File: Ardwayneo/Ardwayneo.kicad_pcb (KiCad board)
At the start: 2 copper layers, 0 parts

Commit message: Setup layout, added track, via, drill presets in design rules
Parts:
- added BT1: Battery 3V, Connector_PinHeader_2.54mm:PinHeader_1x02_P2.54mm_Vertical, F.Cu at (114.0, 65.5)
- added C1: 22pF, Connector_PinHeader_2.54mm:PinHeader_1x09_P2.54mm_Vertical, F.Cu at (98.3, 71.9)
- added C2: 22pF, Connector_PinHeader_2.54mm:PinHeader_1x09_P2.54mm_Vertical, F.Cu at (103.0, 71.9)
- added C3: 10µF, Connector_PinHeader_2.54mm:PinHeader_1x09_P2.54mm_Vertical, F.Cu at (107.6, 71.9)
- added D1: LED, LED_SMD:LED_0805_2012Metric_Pad1.15x1.40mm_HandSolder, F.Cu at (167.1, 88.9)
- added J1: Digital Pins, Connector_PinHeader_2.54mm:PinHeader_1x09_P2.54mm_Vertical, F.Cu at (98.3, 102.4)
- added J2: ICSP, Connector_PinSocket_2.54mm:PinSocket_2x03_P2.54mm_Vertical, F.Cu at (114.7, 102.4)
- added J3: Serial, Connector_PinSocket_2.54mm:PinSocket_1x04_P2.54mm_Vertical, F.Cu at (103.0, 102.4)
- added J4: I²C, Connector_PinSocket_2.54mm:PinSocket_1x04_P2.54mm_Vertical, F.Cu at (107.6, 102.4)
- added R1: 330Ω, Resistor_SMD:R_0805_2012Metric_Pad1.20x1.40mm_HandSolder, F.Cu at (167.0, 92.0)
- added R2: 10KΩ, Resistor_SMD:R_0805_2012Metric_Pad1.20x1.40mm_HandSolder, F.Cu at (172.1, 85.4)
- added U1: 24LC1025, Package_SO:SOIJ-8_5.3x5.3mm_P1.27mm, F.Cu at (170.9, 75.6)
- added U2: 24LC1025, Package_SO:SOIJ-8_5.3x5.3mm_P1.27mm, F.Cu at (159.4, 87.1)
- added U3: ATMEGA328P-AU, digikey-footprints:TQFP-32_7x7mm, F.Cu at (159.9, 77.9)
- added U?1: DS1337S+, Package_SO:SO-8_5.3x6.2mm_P1.27mm, F.Cu at (159.4, 94.4)
- added Y1: Crystal 32MHz, Crystal:Crystal_SMD_MicroCrystal_CC7V-T1A-2Pin_3.2x1.5mm, F.Cu at (167.2, 85.7)
- added Y2: Crystal 16MHz, Crystal:Crystal_SMD_5032-2Pin_5.0x3.2mm_HandSoldering, F.Cu at (170.7, 81.5)
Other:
- net class Power added: clearance 0.2, trace_width 0.3, via_dia 1, via_drill 0.6

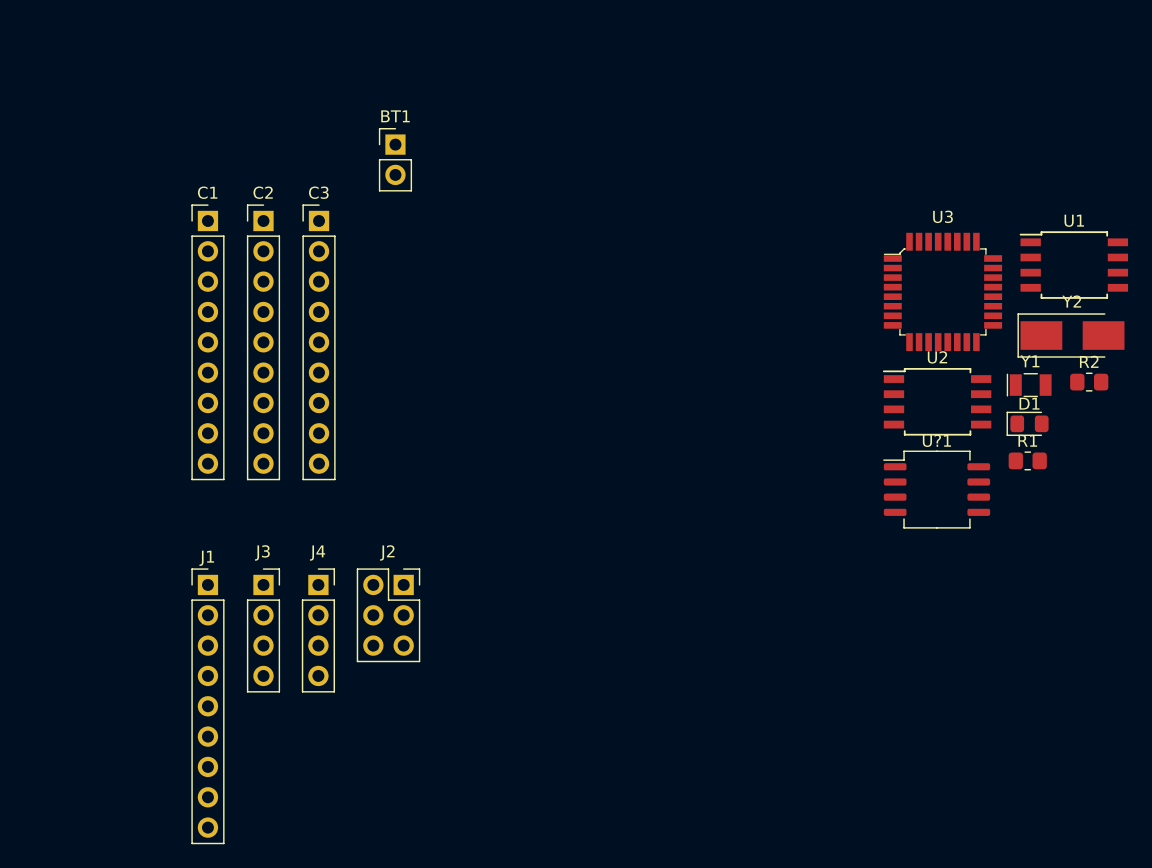
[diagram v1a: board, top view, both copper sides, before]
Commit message: Fixed association for capacitor footprints
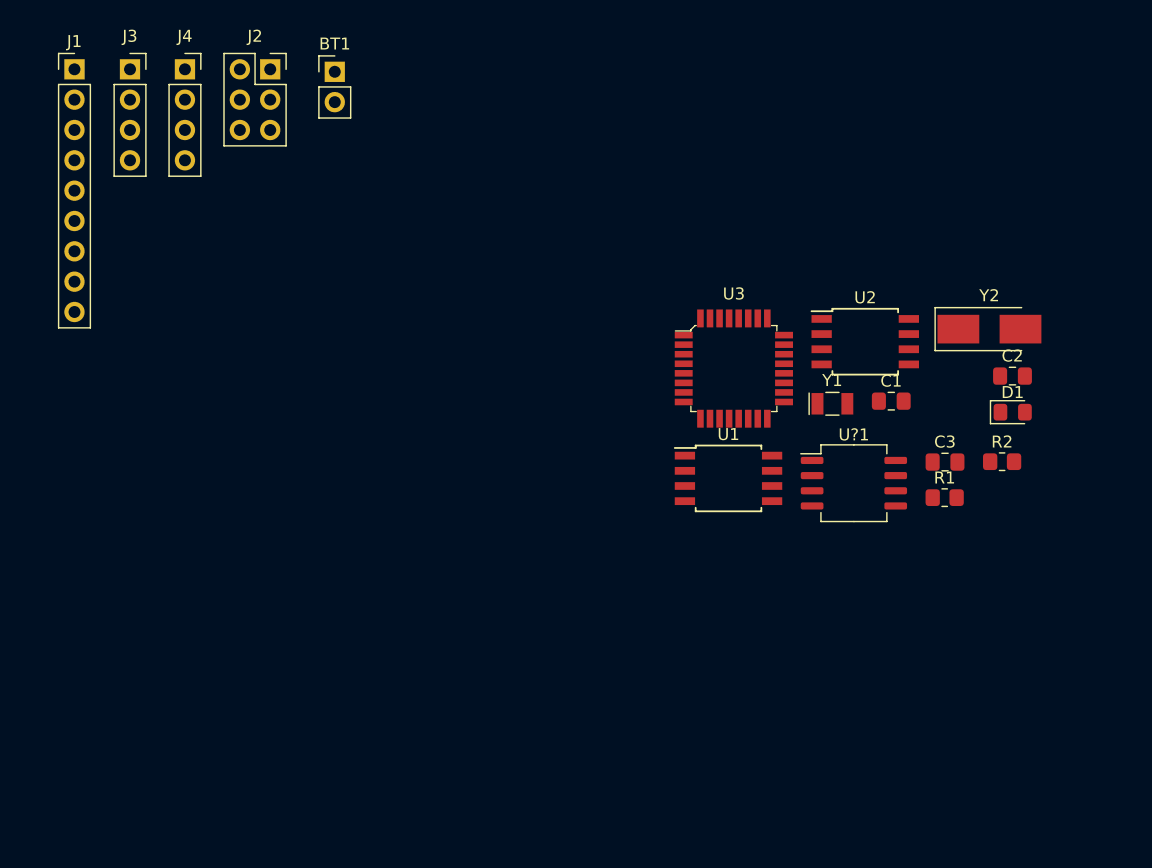
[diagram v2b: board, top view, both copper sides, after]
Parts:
- C1, C2, C3: footprint Connector_PinHeader_2.54mm:PinHeader_1x09_P2.54mm_Vertical -> Capacitor_SMD:C_0805_2012Metric_Pad1.18x1.45mm_HandSolder
- moved C2 64.1 mm to (165.7, 84.9)
- moved C1 59.2 mm to (155.6, 87.0)
- moved C3 56.2 mm to (160.1, 92.1)
- moved J1 44.6 mm to (87.2, 59.2)
- moved J2 44.6 mm to (103.6, 59.2)
- moved J3 44.6 mm to (91.8, 59.2)
- moved J4 44.6 mm to (96.4, 59.2)
- moved U1 34.0 mm to (141.9, 93.5)
- moved U3 18.6 mm to (142.4, 84.3)
- moved Y1 16.7 mm to (150.6, 87.2)
- moved R2 9.88 mm to (164.8, 92.1)
- moved BT1 7.94 mm to (109.0, 59.4)
- moved U2 7.88 mm to (153.4, 82.0)
- moved R1 7.61 mm to (160.0, 95.1)
- moved Y2 6.98 mm to (163.8, 81.0)
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
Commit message: Initial layout distribution
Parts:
- moved R2 76.2 mm to (88.9, 86.4), turned to 90 degrees
- moved Y2 67.7 mm to (96.3, 86.3)
- moved C2 61.3 mm to (104.4, 85.4)
- moved C1 51.2 mm to (104.4, 88.4)
- moved U3 46.8 mm to (97.0, 95.8)
- moved J1 46.2 mm to (95.5, 104.6), turned to 90 degrees
- moved U2 41.4 mm to (112.5, 88.9)
- moved D1 41.1 mm to (126.5, 100.1)
- moved R1 39.2 mm to (121.2, 100.1)
- moved C3 39.1 mm to (121.1, 96.2), turned to 180 degrees
- moved J2 38.7 mm to (87.1, 94.2)
- moved BT1 35.4 mm to (84.6, 85.1)
- moved U1 29.8 mm to (112.5, 98.1)
- moved U3 29.1 mm to (123.7, 89.3)
- moved J4 27.7 mm to (112.8, 81.5), turned to 90 degrees
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- renumbered U?1 to U3

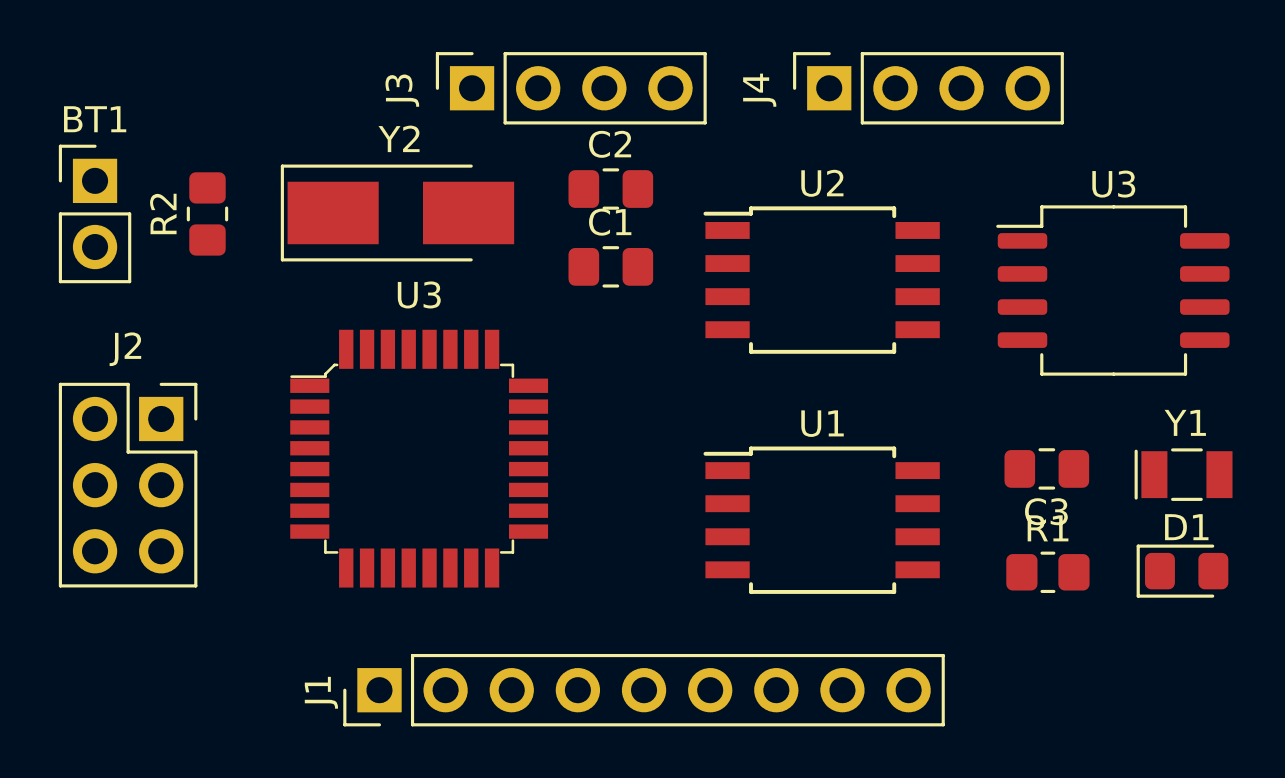
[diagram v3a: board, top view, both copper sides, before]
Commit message: Refined, condensed layout
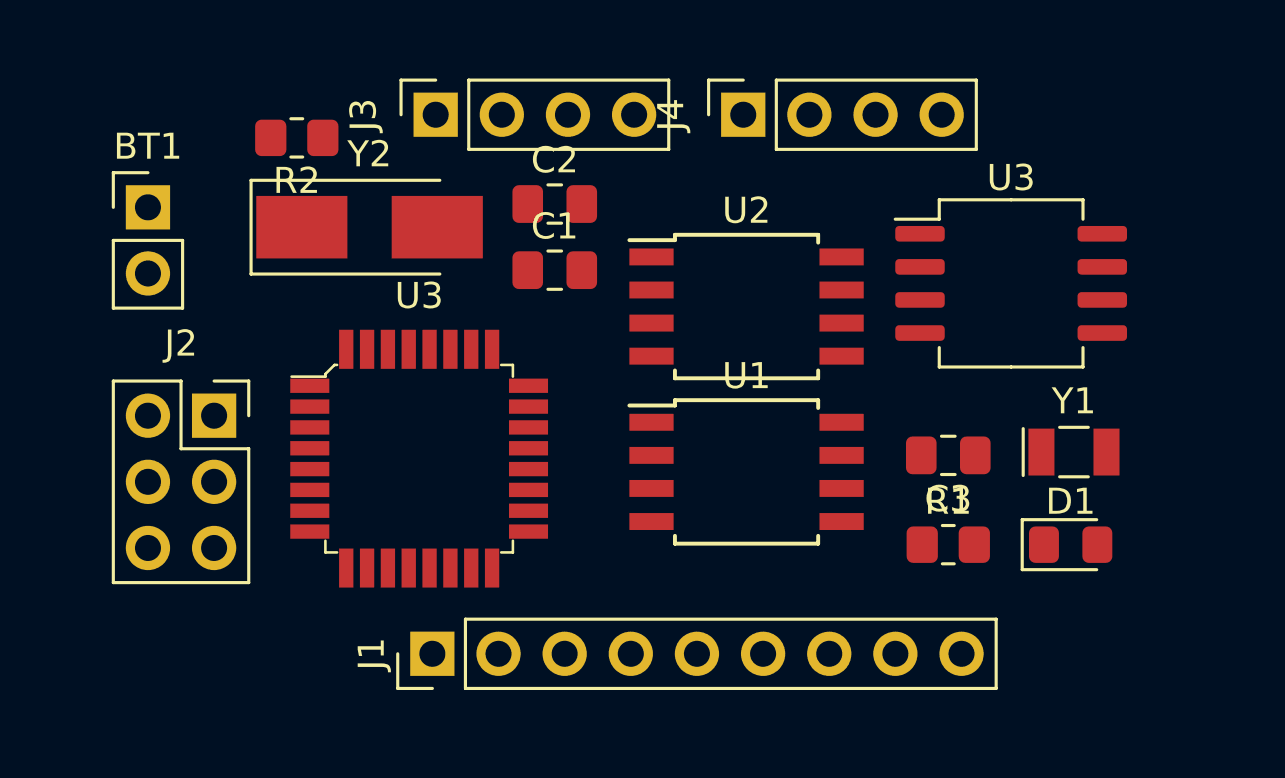
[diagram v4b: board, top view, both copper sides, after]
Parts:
- J4: value I²C -> I2C
- moved D1 4.57 mm to (122.0, 99.1)
- moved R2 4.50 mm to (92.3, 83.4), turned to 180 degrees
- moved Y1 4.42 mm to (122.2, 95.5)
- moved R1 3.97 mm to (117.3, 99.1)
- moved U3 3.95 mm to (119.8, 89.0)
- moved C3 3.82 mm to (117.3, 95.6)
- moved U1 3.46 mm to (109.6, 96.3)
- moved J4 3.45 mm to (109.5, 82.5)
- moved U2 3.09 mm to (109.6, 89.9)
- moved J1 2.47 mm to (97.5, 103.3)
- moved BT1 2.27 mm to (86.6, 86.1)
- moved C2 2.23 mm to (102.2, 86.0)
- moved C1 2.16 mm to (102.2, 88.5)
- moved J2 2.04 mm to (89.2, 94.1)
- moved J3 1.73 mm to (97.7, 82.5)
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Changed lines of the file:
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@@
   )
   (module Connector_PinHeader_2.54mm:PinHeader_1x02_P2.54mm_Vertical (layer F.Cu)
-    (at 84.582 85.09)
+    (at 86.614 86.106)
     (descr "Through hole straight pin header, 1x02, 2.54mm pitch, single row")
     (tags "Through hole pin header THT 1x02 2.54mm single row")
@@
   )
   (module Capacitor_SMD:C_0805_2012Metric_Pad1.18x1.45mm_HandSolder (layer F.Cu)
-    (at 104.389499 88.392)
+    (at 102.235 88.519)
     (descr "Capacitor SMD 0805 (2012 Metric), square (rectangular) end terminal, IPC_7351 nominal with elongated pad for handsoldering. (Body size source: IPC-SM-782 page 76, https://www.pcb-3d.com/wordpress/wp-content/uploads/ipc-sm-782a_amendment_1_and_2.pdf, https://docs.google.com/spreadsheets/d/1BsfQQcO9C6DZCsRaXUlFlo91Tg2WpOkGARC1WS5S8t0/edit?usp=sharing), generated with kicad-footprint-generator")
     (tags "capacitor handsolder")
@@
   )
   (module Capacitor_SMD:C_0805_2012Metric_Pad1.18x1.45mm_HandSolder (layer F.Cu)
-    (at 104.389499 85.403001)
+    (at 102.235 85.979)
     (descr "Capacitor SMD 0805 (2012 Metric), square (rectangular) end terminal, IPC_7351 nominal with elongated pad for handsoldering. (Body size source: IPC-SM-782 page 76, https://www.pcb-3d.com/wordpress/wp-content/uploads/ipc-sm-782a_amendment_1_and_2.pdf, https://docs.google.com/spreadsheets/d/1BsfQQcO9C6DZCsRaXUlFlo91Tg2WpOkGARC1WS5S8t0/edit?usp=sharing), generated with kicad-footprint-generator")
     (tags "capacitor handsolder")
@@
   )
   (module Capacitor_SMD:C_0805_2012Metric_Pad1.18x1.45mm_HandSolder (layer F.Cu)
-    (at 121.132 96.151 180)
+    (at 117.348 95.631 180)
     (descr "Capacitor SMD 0805 (2012 Metric), square (rectangular) end terminal, IPC_7351 nominal with elongated pad for handsoldering. (Body size source: IPC-SM-782 page 76, https://www.pcb-3d.com/wordpress/wp-content/uploads/ipc-sm-782a_amendment_1_and_2.pdf, https://docs.google.com/spreadsheets/d/1BsfQQcO9C6DZCsRaXUlFlo91Tg2WpOkGARC1WS5S8t0/edit?usp=sharing), generated with kicad-footprint-generator")
     (tags "capacitor handsolder")
@@
   )
   (module LED_SMD:LED_0805_2012Metric_Pad1.15x1.40mm_HandSolder (layer F.Cu)
-    (at 126.501 100.076)
+    (at 122.047 99.06)
     (descr "LED SMD 0805 (2012 Metric), square (rectangular) end terminal, IPC_7351 nominal, (Body size source: https://docs.google.com/spreadsheets/d/1BsfQQcO9C6DZCsRaXUlFlo91Tg2WpOkGARC1WS5S8t0/edit?usp=sharing), generated with kicad-footprint-generator")
     (tags "LED handsolder")
@@
   )
   (module Connector_PinHeader_2.54mm:PinHeader_1x09_P2.54mm_Vertical (layer F.Cu)
-    (at 95.504 104.648 90)
+    (at 97.536 103.251 90)
     (descr "Through hole straight pin header, 1x09, 2.54mm pitch, single row")
     (tags "Through hole pin header THT 1x09 2.54mm single row")
@@
   )
   (module Connector_PinSocket_2.54mm:PinSocket_2x03_P2.54mm_Vertical (layer F.Cu)
-    (at 87.122 94.234)
+    (at 89.154 94.107)
     (descr "Through hole straight socket strip, 2x03, 2.54mm pitch, double cols (from Kicad 4.0.7), script generated")
     (tags "Through hole socket strip THT 2x03 2.54mm double row")
@@
   )
   (module Connector_PinSocket_2.54mm:PinSocket_1x04_P2.54mm_Vertical (layer F.Cu)
-    (at 99.06 81.534 90)
+    (at 97.663 82.55 90)
     (descr "Through hole straight socket strip, 1x04, 2.54mm pitch, single row (from Kicad 4.0.7), script generated")
     (tags "Through hole socket strip THT 1x04 2.54mm single row")
@@
   )
   (module Connector_PinSocket_2.54mm:PinSocket_1x04_P2.54mm_Vertical (layer F.Cu)
-    (at 112.776 81.534 90)
+    (at 109.474 82.55 90)
     (descr "Through hole straight socket strip, 1x04, 2.54mm pitch, single row (from Kicad 4.0.7), script generated")
     (tags "Through hole socket strip THT 1x04 2.54mm single row")
@@
       (effects (font (size 1 1) (thickness 0.15)))
     )
-    (fp_text value I²C (at 0 10.39 90) (layer F.Fab)
+    (fp_text value I2C (at 0 10.39 90) (layer F.Fab)
       (effects (font (size 1 1) (thickness 0.15)))
     )
@@
   )
   (module Resistor_SMD:R_0805_2012Metric_Pad1.20x1.40mm_HandSolder (layer F.Cu)
-    (at 121.174 100.121)
+    (at 117.348 99.06)
     (descr "Resistor SMD 0805 (2012 Metric), square (rectangular) end terminal, IPC_7351 nominal with elongated pad for handsoldering. (Body size source: IPC-SM-782 page 72, https://www.pcb-3d.com/wordpress/wp-content/uploads/ipc-sm-782a_amendment_1_and_2.pdf), generated with kicad-footprint-generator")
     (tags "resistor handsolder")
@@
   )
   (module Resistor_SMD:R_0805_2012Metric_Pad1.20x1.40mm_HandSolder (layer F.Cu)
-    (at 88.9 86.36 90)
+    (at 92.329 83.439 180)
     (descr "Resistor SMD 0805 (2012 Metric), square (rectangular) end terminal, IPC_7351 nominal with elongated pad for handsoldering. (Body size source: IPC-SM-782 page 72, https://www.pcb-3d.com/wordpress/wp-content/uploads/ipc-sm-782a_amendment_1_and_2.pdf), generated with kicad-footprint-generator")
     (tags "resistor handsolder")
     (attr smd)
-    (fp_text reference R2 (at 0 -1.65 90) (layer F.SilkS)
-      (effects (font (size 1 1) (thickness 0.15)))
-    )
-    (fp_text value 10KΩ (at 0 1.65 90) (layer F.Fab)
-      (effects (font (size 1 1) (thickness 0.15)))
-    )
-    (fp_text user %R (at 0 0 90) (layer F.Fab)
+    (fp_text reference R2 (at 0 -1.65) (layer F.SilkS)
+      (effects (font (size 1 1) (thickness 0.15)))
+    )
+    (fp_text value 10KΩ (at 0 1.65) (layer F.Fab)
+      (effects (font (size 1 1) (thickness 0.15)))
+    )
+    (fp_text user %R (at 0 0) (layer F.Fab)
       (effects (font (size 0.5 0.5) (thickness 0.08)))
     )
@@
     (fp_line (start 1.85 -0.95) (end 1.85 0.95) (layer F.CrtYd) (width 0.05))
     (fp_line (start 1.85 0.95) (end -1.85 0.95) (layer F.CrtYd) (width 0.05))
-    (pad 2 smd roundrect (at 1 0 90) (size 1.2 1.4) (layers F.Cu F.Paste F.Mask) (roundrect_rratio 0.208333)
+    (pad 2 smd roundrect (at 1 0 180) (size 1.2 1.4) (layers F.Cu F.Paste F.Mask) (roundrect_rratio 0.208333)
       (net 16 /RESET))
-    (pad 1 smd roundrect (at -1 0 90) (size 1.2 1.4) (layers F.Cu F.Paste F.Mask) (roundrect_rratio 0.208333)
+    (pad 1 smd roundrect (at -1 0 180) (size 1.2 1.4) (layers F.Cu F.Paste F.Mask) (roundrect_rratio 0.208333)
       (net 1 /Vcc))
     (model ${KISYS3DMOD}/Resistor_SMD.3dshapes/R_0805_2012Metric.wrl
@@
   )
   (module Package_SO:SOIJ-8_5.3x5.3mm_P1.27mm (layer F.Cu)
-    (at 112.522 98.121)
+    (at 109.601 96.266)
     (descr "8-Lead Plastic Small Outline (SM) - Medium, 5.28 mm Body [SOIC] (see Microchip Packaging Specification 00000049BS.pdf)")
     (tags "SOIC 1.27")
@@
   )
   (module Package_SO:SOIJ-8_5.3x5.3mm_P1.27mm (layer F.Cu)
-    (at 112.522 88.9)
+    (at 109.601 89.916)
     (descr "8-Lead Plastic Small Outline (SM) - Medium, 5.28 mm Body [SOIC] (see Microchip Packaging Specification 00000049BS.pdf)")
     (tags "SOIC 1.27")
@@
   )
   (module Package_SO:SO-8_5.3x6.2mm_P1.27mm (layer F.Cu)
-    (at 123.698 89.3)
+    (at 119.761 89.027)
     (descr "SO, 8 Pin (https://www.ti.com/lit/ml/msop001a/msop001a.pdf), generated with kicad-footprint-generator ipc_gullwing_generator.py")
     (tags "SO SO")
@@
   )
   (module Crystal:Crystal_SMD_MicroCrystal_CC7V-T1A-2Pin_3.2x1.5mm (layer F.Cu)
-    (at 126.512 96.371)
+    (at 122.174 95.504)
     (descr "SMD Crystal MicroCrystal CC7V-T1A/CM7V-T1A series https://www.microcrystal.com/fileadmin/Media/Products/32kHz/Datasheet/CC7V-T1A.pdf, 3.2x1.5mm^2 package")
     (tags "SMD SMT crystal")
@@
   )
   (module Crystal:Crystal_SMD_5032-2Pin_5.0x3.2mm_HandSoldering (layer F.Cu)
-    (at 96.326 86.323001)
+    (at 95.123 86.868)
     (descr "SMD Crystal SERIES SMD2520/2 http://www.icbase.com/File/PDF/HKC/HKC00061008.pdf, hand-soldering, 5.0x3.2mm^2 package")
     (tags "SMD SMT crystal hand-soldering")

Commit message: Refined layout
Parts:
- moved U3 1.05 mm to (98.0, 95.5)
- moved J1 0.28 mm to (97.4, 103.5)
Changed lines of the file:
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@@
   )
   (module Connector_PinHeader_2.54mm:PinHeader_1x09_P2.54mm_Vertical (layer F.Cu)
-    (at 97.536 103.251 90)
+    (at 97.409 103.505 90)
     (descr "Through hole straight pin header, 1x09, 2.54mm pitch, single row")
     (tags "Through hole pin header THT 1x09 2.54mm single row")
@@
   )
   (module digikey-footprints:TQFP-32_7x7mm (layer F.Cu)
-    (at 97.028 95.758)
+    (at 98.044 95.504)
     (descr http://www.atmel.com/Images/Atmel-8826-SEEPROM-PCB-Mounting-Guidelines-Surface-Mount-Packages-ApplicationNote.pdf)
     (attr smd)
